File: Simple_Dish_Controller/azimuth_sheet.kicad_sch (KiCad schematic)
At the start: 19 parts, among them J3 DA15_Socket, J4 CRJ022-G-TH, Q3 PZT2222A, Q4 PZT2222A, SW3 SW_SPDT_312, U2 74LS08, U3 74LS32, U5 ICM7555xP

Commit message: Added RJ45 ports
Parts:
- removed J3: DA15_Socket, Connector_Dsub:DSUB-15_Socket_Horizontal_P2.77x2.54mm_EdgePinOffset9.40mm, symbol Connector:DA15_Socket
- removed J4: CRJ022-G-TH, CRJ022-G-TH:CUI_CRJ022-G-TH, symbol CRJ022-G-TH:CRJ022-G-TH
- added J3: 1-Pin Terminal Block, RHDR1W160P0X826_1X1_1020X1270X1270P, symbol 1-Pin Barrier Terminal Block:38700-6301
- added J5: CRJ022-G-TH, CRJ022-G-TH:CUI_CRJ022-G-TH, symbol CRJ022-G-TH:CRJ022-G-TH
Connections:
- net +5V: now also J5.1L, J5.1R
- net Dir: now also J5.4R
- net GND: now also J5.2L, J5.2R
- net Limit Sw1: now also J5.3L
- net Limit Sw2: now also J5.4L
- net Pul: now also J5.3R
- net Pulse Enable: now reaches U3.6, U5.4 (R)
- new net Shield: J3.1, J5.S1 (SHIELD), J5.S2 (SHIELD__1), J5.S3 (SHIELD__2)
- no-connect marks 7 -> 8
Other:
- note added: "Azimuth Moror Control"
- note added: "Connect to Chassis"
- note added: "RJ45 Ports"
- note added: "Shield to Chassis"
- moved on the sheet: C6, C7, Q3, Q4, R14, R15, R16, R18, R19, R7, R8, R9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

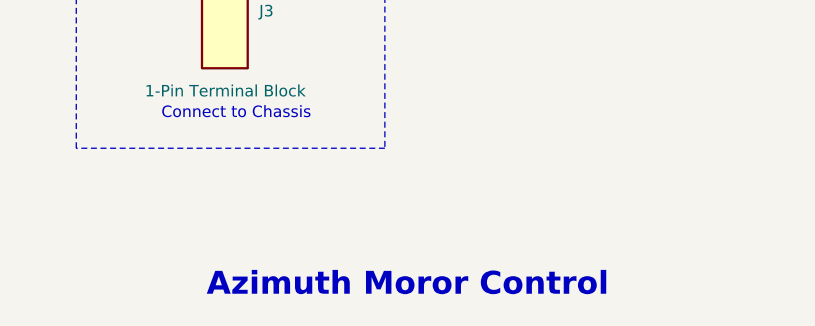
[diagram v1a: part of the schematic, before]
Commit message: Footprints defined - passes ERC
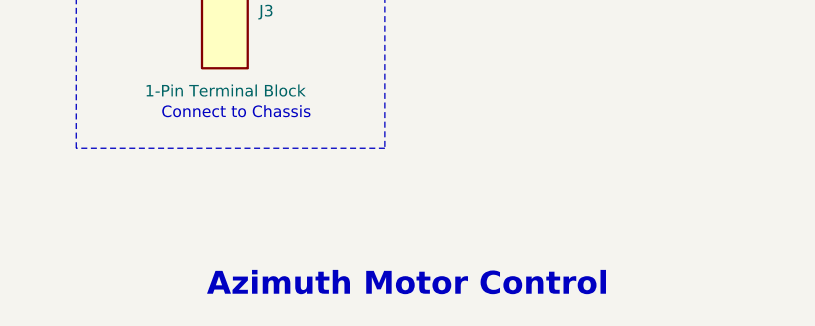
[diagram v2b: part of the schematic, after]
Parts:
- J3: footprint RHDR1W160P0X826_1X1_1020X1270X1270P -> 2-port JR45:CUI_CRJ022-G-TH
- J5: footprint CRJ022-G-TH:CUI_CRJ022-G-TH -> 2-port JR45:CUI_CRJ022-G-TH
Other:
- note added: "Azimuth Motor Control"
- note removed: "Azimuth Moror Control"
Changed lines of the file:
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@@
 		)
 	)
-	(text "Azimuth Moror Control"
+	(text "Azimuth Motor Control"
 		(exclude_from_sim no)
 		(at 201.93 171.45 0)
@@
 			)
 		)
-		(property "Footprint" "CRJ022-G-TH:CUI_CRJ022-G-TH"
+		(property "Footprint" "2-port JR45:CUI_CRJ022-G-TH"
 			(at 254 99.06 0)
 			(effects
@@
 			)
 		)
-		(property "Description" ""
+		(property "Description" "2-port JR45"
 			(at 254 99.06 0)
 			(effects
@@
 			)
 		)
-		(property "Footprint" "CRJ022-G-TH:CUI_CRJ022-G-TH"
+		(property "Footprint" "2-port JR45:CUI_CRJ022-G-TH"
 			(at 254 60.96 0)
 			(effects
@@
 			)
 		)
-		(property "Description" ""
+		(property "Description" "2-port JR45"
 			(at 254 60.96 0)
 			(effects
@@
 			)
 		)
-		(property "Footprint" "RHDR1W160P0X826_1X1_1020X1270X1270P"
+		(property "Footprint" "2-port JR45:CUI_CRJ022-G-TH"
 			(at 86.69 148.59 0)
 			(effects

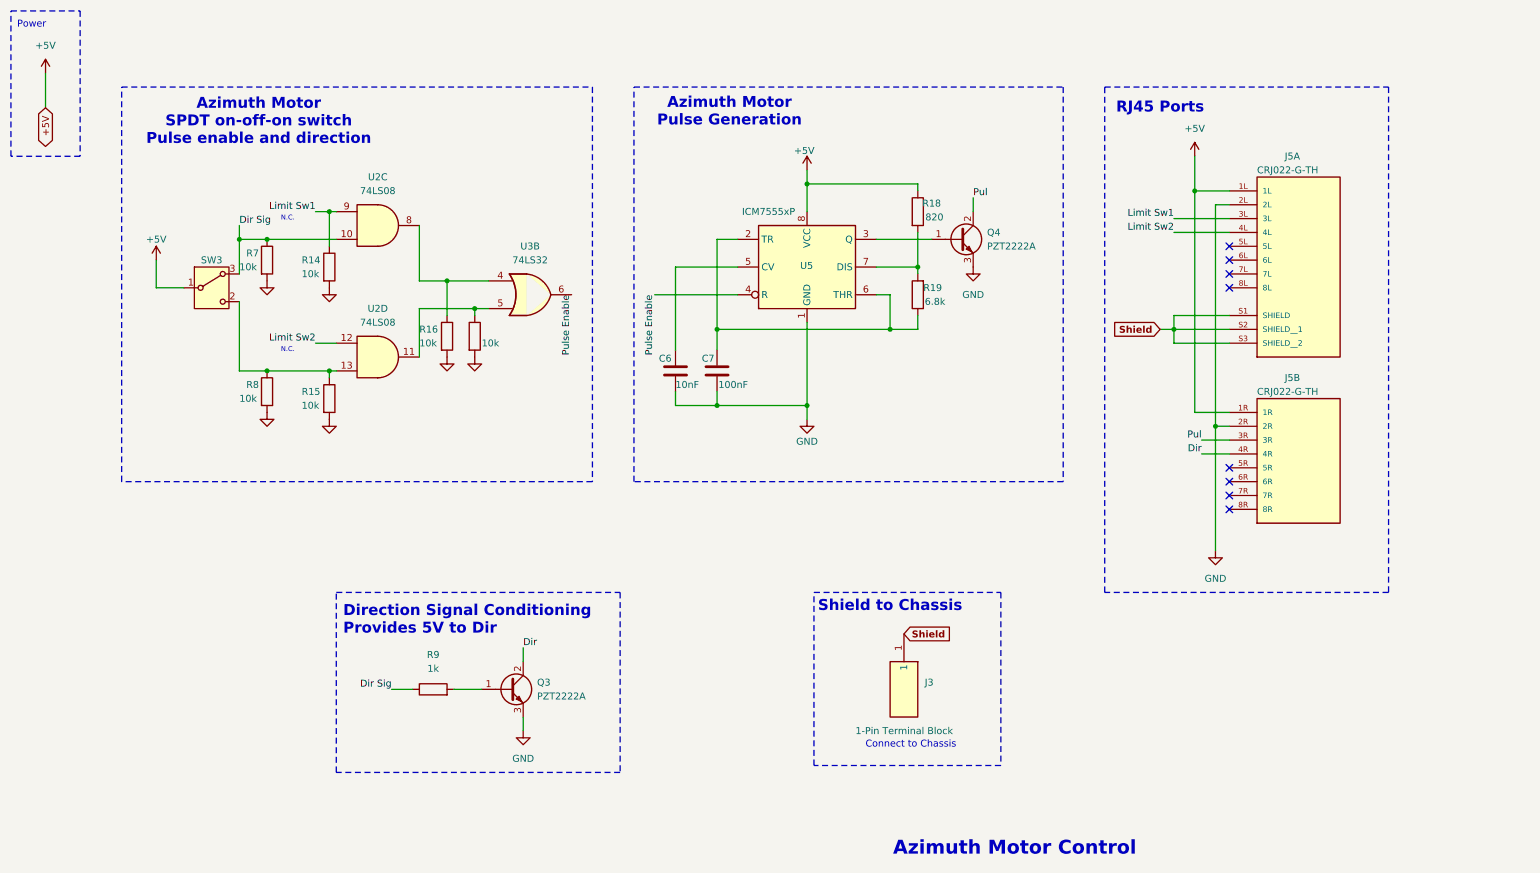
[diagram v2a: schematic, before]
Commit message: 777 chip is now SMD
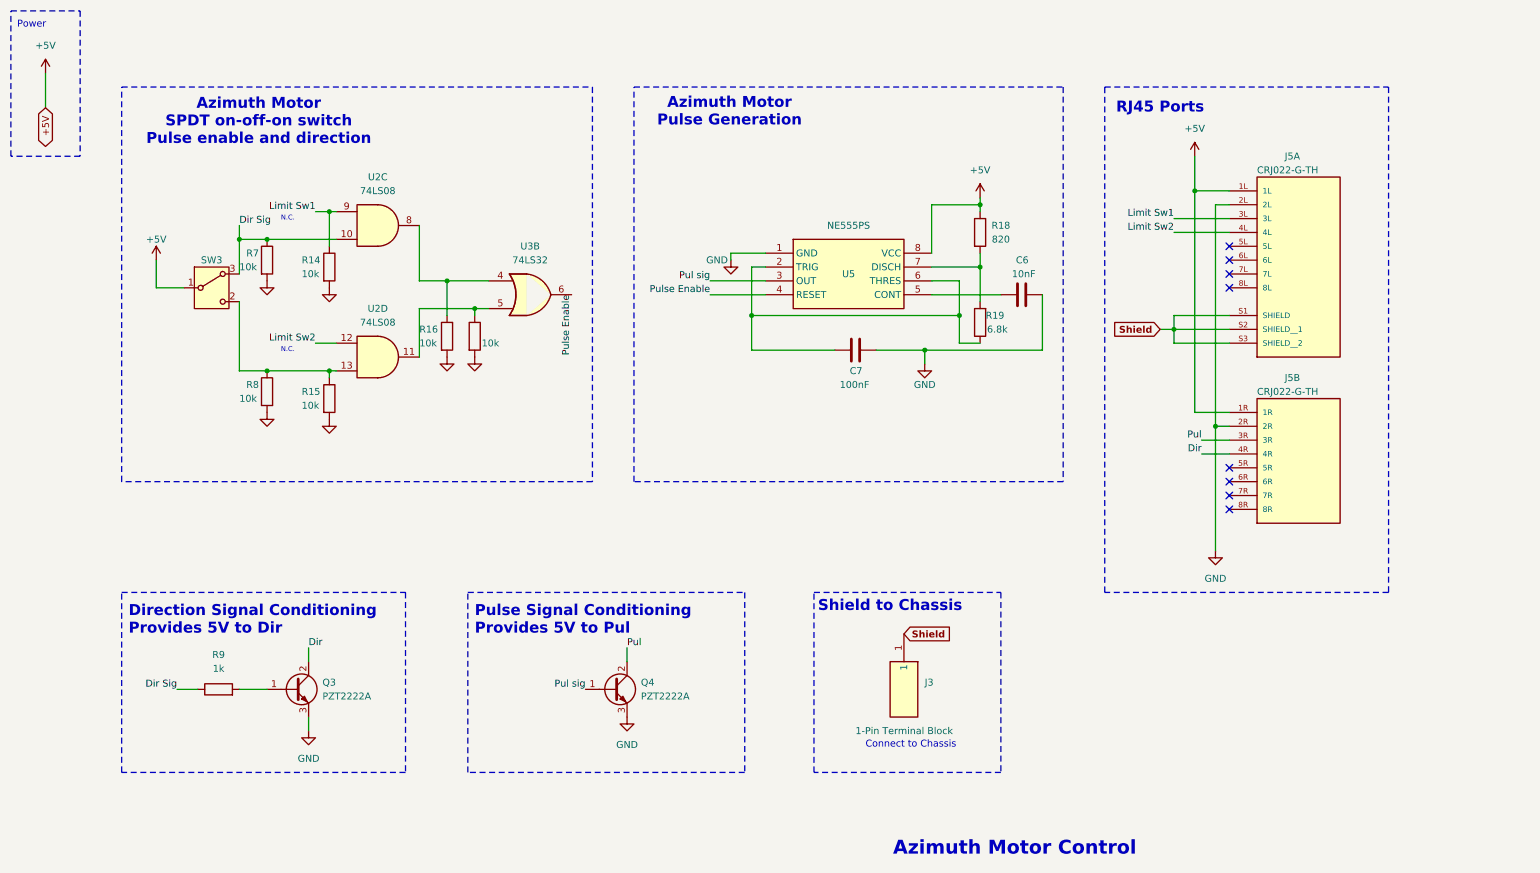
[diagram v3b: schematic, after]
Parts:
- removed U5: ICM7555xP, Package_DIP:DIP-8_W7.62mm, symbol Timer:ICM7555xP
- added U5: NE555PS, NE555P Osc Chip SMD:SOIC127P780X200-8N, symbol NE555P Osc Chip SMD:NE555PS
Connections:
- net +5V: now also U5.8 (VCC)
- net GND: now also U5.1 (GND)
- net Pulse Enable: now also U5.4 (RESET)
- net at R18.2, R19.2: now also U5.7 (DISCH)
- net at C7.1, R19.1: now also U5.2 (TRIG), U5.6 (THRES)
- net Pul sig: now reaches Q4.1 (B)
- net Pul sig: now also U5.3 (OUT)
- net at C6.1: now also U5.5 (CONT)
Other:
- note added: "Pulse Signal Conditioning Provides 5V to Pul"
- moved on the sheet: Q3, R9

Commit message: Added parts dir
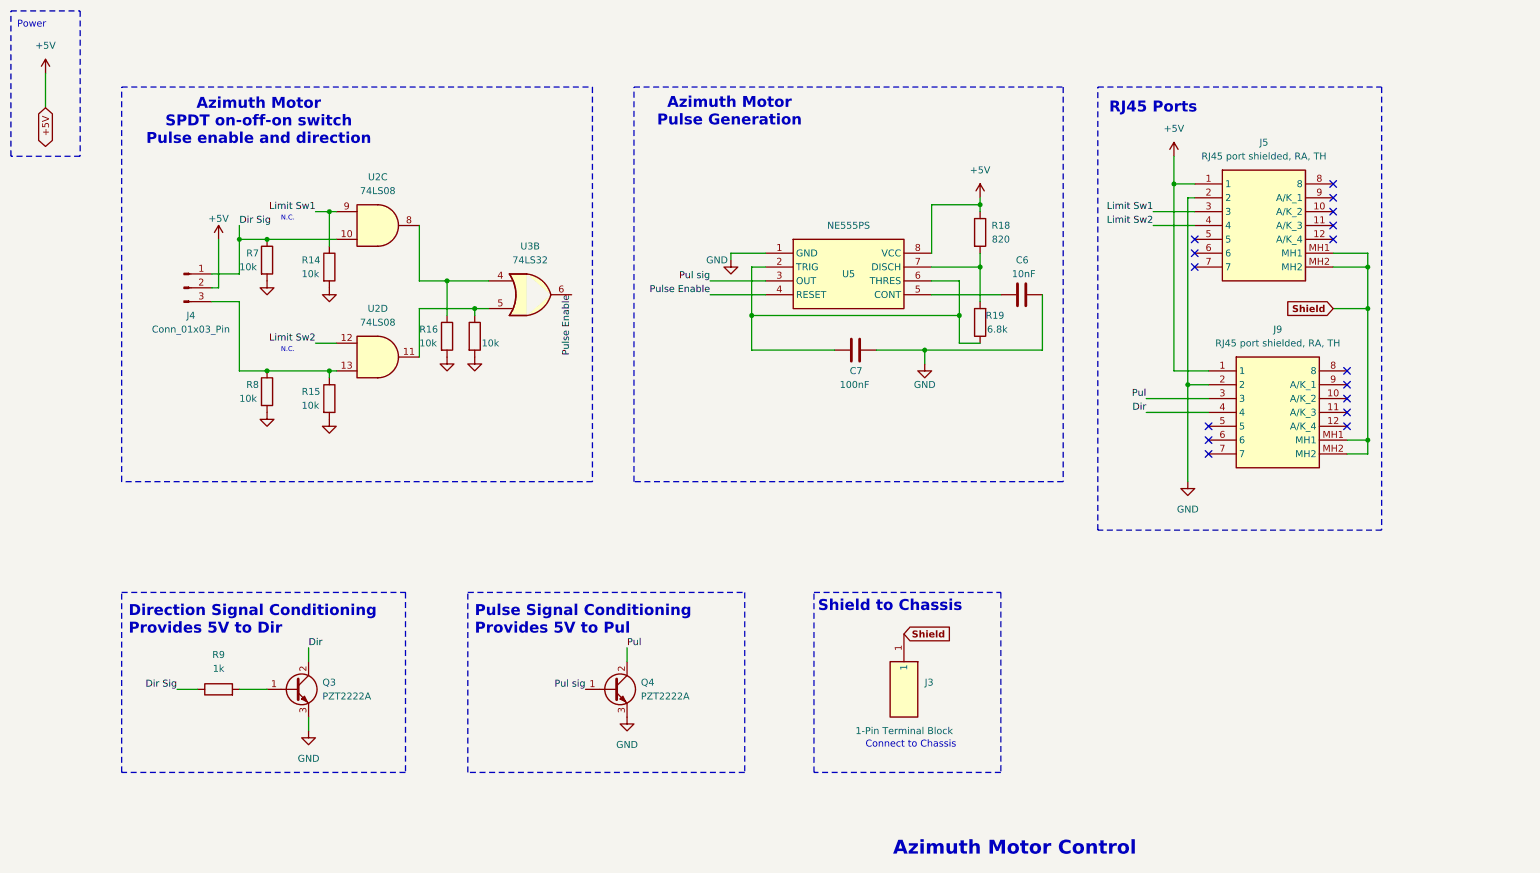
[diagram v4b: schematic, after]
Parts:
- removed J5: CRJ022-G-TH, 2-port JR45:CUI_CRJ022-G-TH, symbol CRJ022-G-TH:CRJ022-G-TH
- removed SW3: SW_SPDT_312, symbol Switch:SW_SPDT_312
- added J4: Conn_01x03_Pin, Connector_PinHeader_2.54mm:PinHeader_1x03_P2.54mm_Vertical, symbol Connector:Conn_01x03_Pin
- added J5, J9: RJ45 port shielded, RA, TH, DishController_footprints:RJ45 Port Shielded, Right Angle TH, symbol DishController_symbols:RJ45 port shielded, Right Angle TH
- C6, C7: footprint (none) -> Capacitor_SMD:C_0805_2012Metric
- J3: footprint 2-port JR45:CUI_CRJ022-G-TH -> 1-Pin Barrier Terminal Block:RHDR1W160P0X826_1X1_1020X1270X1270P
- R14, R15, R16, R17, R18, R19, R7, R8, R9: footprint (none) -> Resistor_SMD:R_0805_2012Metric
- U2: footprint (none) -> 74LS08_SOIC:SOIC127P600X175-14N
- U3: footprint (none) -> 74LS32_SOIC:SOIC127P600X175-14N
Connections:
- net +5V: now also J4.2 (Pin_2), J5.1, J9.1
- net Dir: now also J9.4
- net Dir Sig: now also J4.1 (Pin_1)
- net GND: now also J5.2, J9.2
- net Limit Sw1: now also J5.3
- net Limit Sw2: now also J5.4
- net Pul: now also J9.3
- net Shield: now also J5.MH1, J5.MH2, J9.MH1, J9.MH2
- net at R15.1, R8.1, U2.13: now also J4.3 (Pin_3)
- no-connect marks 8 -> 16

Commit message: Still creating parts libraries
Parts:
- removed J4: Conn_01x03_Pin, Connector_PinHeader_2.54mm:PinHeader_1x03_P2.54mm_Vertical, symbol Connector:Conn_01x03_Pin
- added J4: Conn_01x03_Pin, DishFootprints:PinHeader_1x03_P2.54mm_Vertical, symbol DishSymbols:Conn_01x03_Pin
- renumbered U2 to a
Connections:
- net +5V: now also J4.2
- net Dir Sig: now also J4.1
- net at R15.1, R8.1, U2.13: now also J4.3
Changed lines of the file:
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@@
+	)
+	(symbol
+		(lib_id "DishSymbols:Conn_01x03_Pin")
+		(at 49.53 68.58 0)
+		(unit 1)
+		(exclude_from_sim no)
+		(in_bom yes)
+		(on_board yes)
+		(dnp no)
+		(property "Reference" "J4"
+			(at 50.8 63.5 0)
+			(effects
+				(font
+					(size 1.27 1.27)
+				)
+			)
+		)
+		(property "Value" "Conn_01x03_Pin"
+			(at 50.8 73.66 0)
+			(effects
+				(font
+					(size 1.27 1.27)
+				)
+			)
+		)
+		(property "Footprint" "DishFootprints:PinHeader_1x03_P2.54mm_Vertical"
+			(at 49.53 68.58 0)
+			(effects
+				(font
+					(size 1.27 1.27)
+				)
+				(hide yes)
+			)
+		)
+		(property "Datasheet" "~https://app.adam-tech.com/products/download/data_sheet/201605/ph1-xx-ua-data-sheet.pdf"
+			(at 49.53 68.58 0)
+			(effects
+				(font
+					(size 1.27 1.27)
+				)
+				(hide yes)
+			)
+		)
+		(property "Description" "Connector Header Through Hole 3 position 0.100\" (2.54mm)"
+			(at 49.53 68.58 0)
+			(effects
+				(font
+					(size 1.27 1.27)
+				)
+				(hide yes)
+			)
+		)
+		(property "Package" "-"
+			(at 49.53 68.58 0)
+			(effects
+				(font
+					(size 1 1)
+				)
+				(hide yes)
+			)
+		)
+		(property "MF" "Adam Tech"
+			(at 49.53 68.58 0)
+			(effects
+				(font
+					(size 1 1)
+				)
+				(hide yes)
+			)
+		)
+		(property "MPN" "PH1-03-UA"
+			(at 49.53 68.58 0)
+			(effects
+				(font
+					(size 1 1)
+				)
+				(hide yes)
+			)
+		)
+		(property "DIS" "Digikey"
+			(at 49.53 68.58 0)
+			(effects
+				(font
+					(size 1 1)
+				)
+				(hide yes)
+			)
+		)
+		(property "DPN" "2057-PH1-03-UA-ND"
+			(at 49.53 68.58 0)
+			(effects
+				(font
+					(size 1 1)
+				)
+				(hide yes)
+			)
+		)
+		(property "Purchase_URL" "https://www.digikey.com/en/products/detail/adam-tech/PH1-03-UA/9830289"
+			(at 49.53 68.58 0)
+			(effects
+				(font
+					(size 1 1)
+				)
+				(hide yes)
+			)
+		)
+		(property "Price" "0.04"
+			(at 49.53 68.58 0)
+			(effects
+				(font
+					(size 1 1)
+				)
+				(hide yes)
+			)
+		)
+		(property "Note" ""
+			(at 49.53 68.58 0)
+			(effects
+				(font
+					(size 1 1)
+				)
+				(hide yes)
+			)
+		)
+		(pin "2"
+		)
+		(pin "3"
+		)
+		(pin "1"
+		)
+		(instances
+			(project ""
+				(path "/8648ccd3-30ce-4b98-baff-aeab56a7c9f5/809ce83c-7739-411d-92b7-06d9bcd34d12"
+					(reference "J4")
+					(unit 1)
+				)
+			)
+		)
 	)
 	(symbol
@@
 		(dnp no)
 		(fields_autoplaced yes)
-		(property "Reference" "U2"
+		(property "Reference" "a"
 			(at 85.0817 48.26 0)
 			(effects
@@
 			(project "simple_dish_manual_controller"
 				(path "/8648ccd3-30ce-4b98-baff-aeab56a7c9f5/809ce83c-7739-411d-92b7-06d9bcd34d12"
-					(reference "U2")
+					(reference "a")
 					(unit 3)
 				)
@@
 					(unit 1)
 				)
-			)
-		)
-	)
-	(symbol
-		(lib_id "Connector:Conn_01x03_Pin")
-		(at 49.53 68.58 0)
-		(unit 1)
-		(exclude_from_sim no)
-		(in_bom yes)
-		(on_board yes)
-		(dnp no)
-		(property "Reference" "J4"
-			(at 50.8 73.66 0)
-			(effects
-				(font
-					(size 1.27 1.27)
-				)
-			)
-		)
-		(property "Value" "Conn_01x03_Pin"
-			(at 50.8 76.2 0)
-			(effects
-				(font
-					(size 1.27 1.27)
-				)
-			)
-		)
-		(property "Footprint" "Connector_PinHeader_2.54mm:PinHeader_1x03_P2.54mm_Vertical"
-			(at 49.53 68.58 0)
-			(effects
-				(font
-					(size 1.27 1.27)
-				)
-				(hide yes)
-			)
-		)
-		(property "Datasheet" "~"
-			(at 49.53 68.58 0)
-			(effects
-				(font
-					(size 1.27 1.27)
-				)
-				(hide yes)
-			)
-		)
-		(property "Description" "Generic connector, single row, 01x03, script generated"
-			(at 49.53 68.58 0)
-			(effects
-				(font
-					(size 1.27 1.27)
-				)
-				(hide yes)
-			)
-		)
-		(pin "3"
-		)
-		(pin "1"
-		)
-		(pin "2"
-		)
-		(instances
-			(project ""
-				(path "/8648ccd3-30ce-4b98-baff-aeab56a7c9f5/809ce83c-7739-411d-92b7-06d9bcd34d12"
-					(reference "J4")
-					(unit 1)
-				)
